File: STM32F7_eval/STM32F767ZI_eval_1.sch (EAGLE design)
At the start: 102 parts, among them CN1 STLINKV2_SWD_IF_, CN2 GROVE-4P-CONN-I2C-90D, CN3 GROVE-4P-CONN-I2C-90D, CN5 ARDUINO_COMPAT_IF, CN7 WFT0750CZ09-SMD_, CN9 UART_IF, Q1 PMF370XN_, SW1 SKRPACE010_, SW2 SKRPACE010_, U1 STM32F767ZI_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

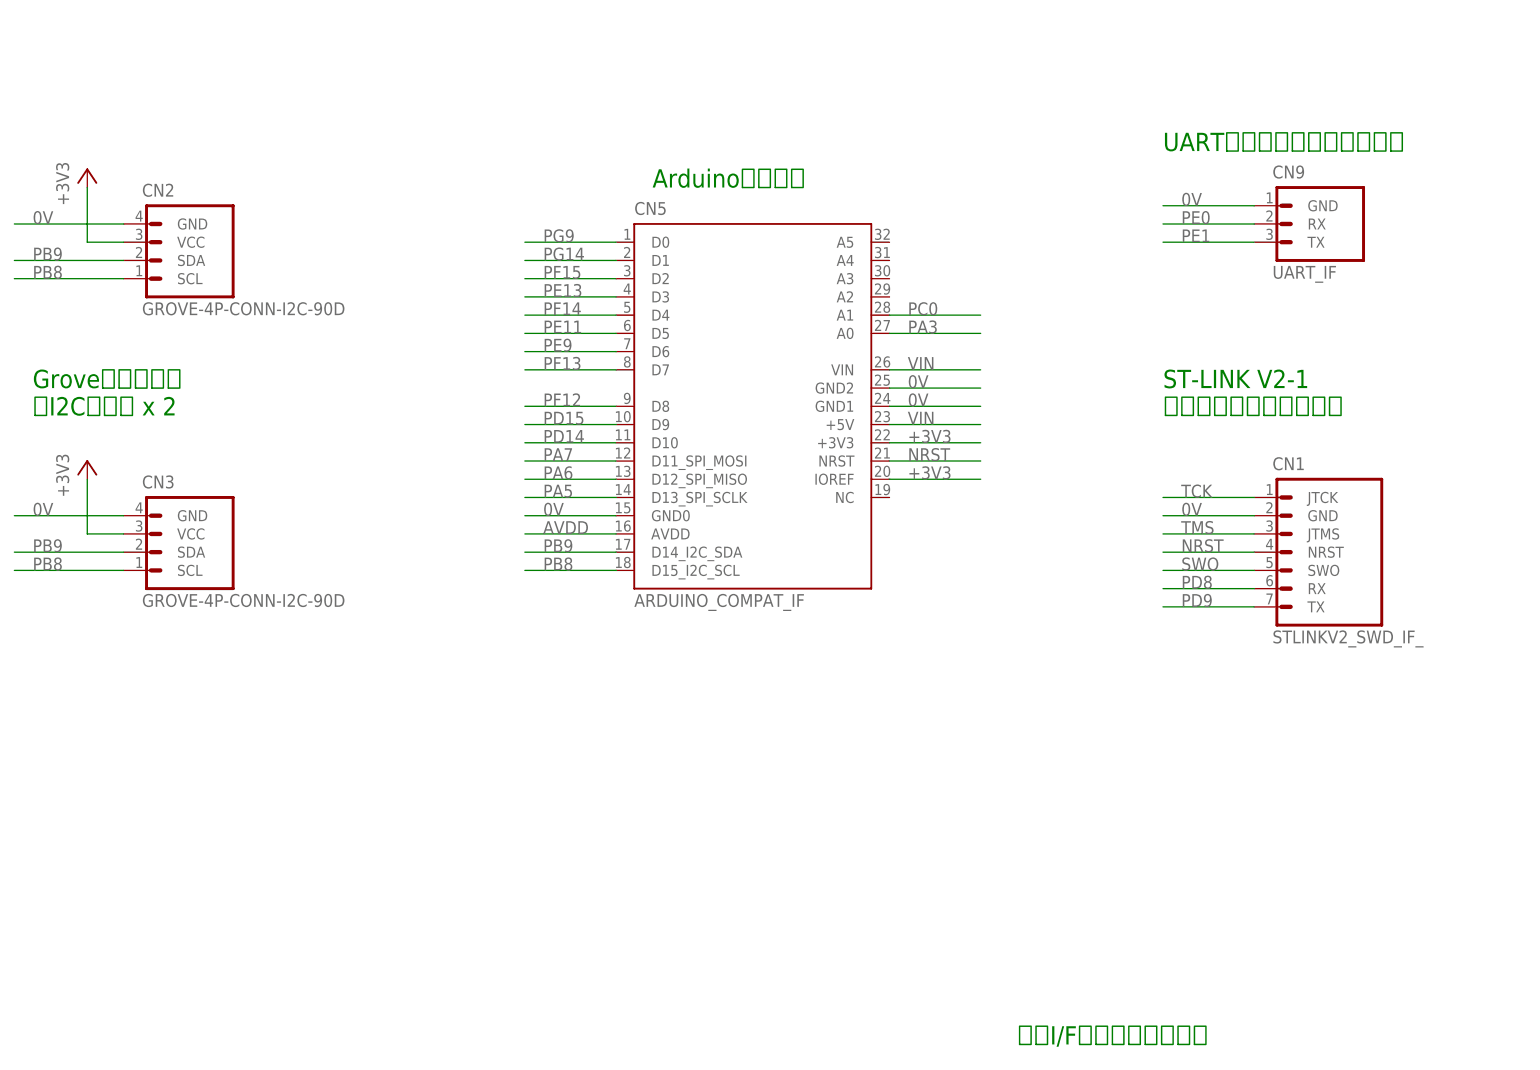
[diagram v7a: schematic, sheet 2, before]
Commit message: レイアウトを修正
・外部RX、TXはArduinoアナログピンを流用させるよう実装変更
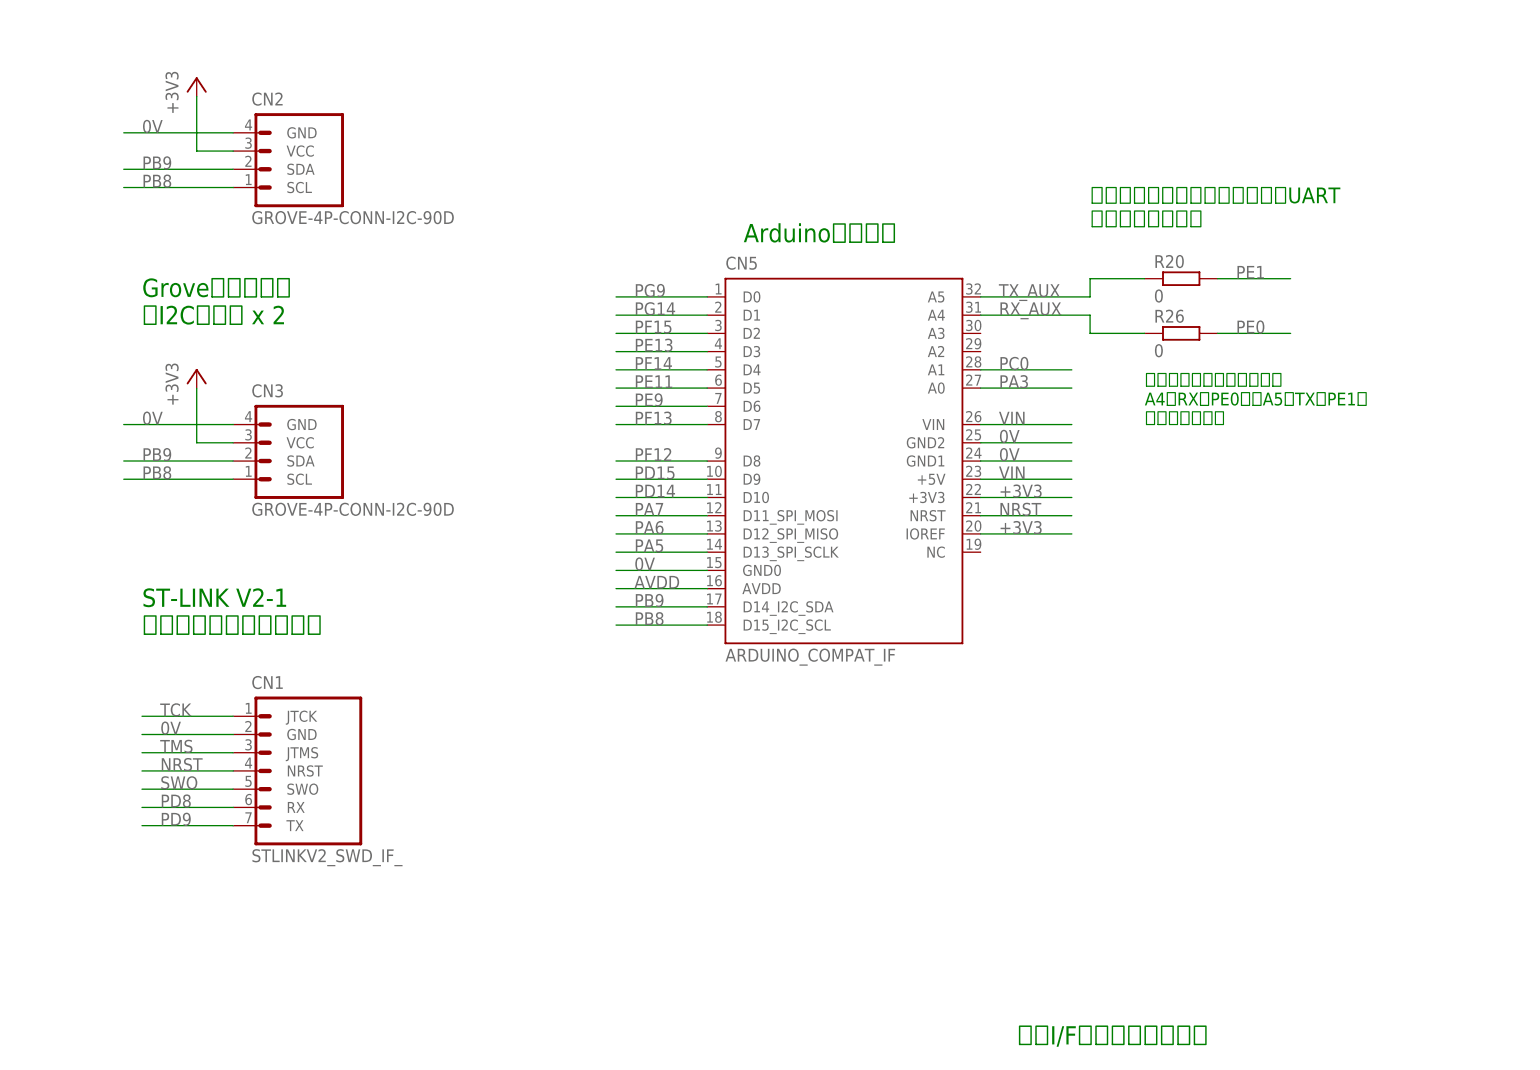
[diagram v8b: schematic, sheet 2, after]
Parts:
- removed CN9: UART_IF, PartsForProto:UART_IF
- added R20, R26: 0, Parts:RESISTOR_0603_DEV
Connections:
- new net RX_AUX: CN5.A4, R26.1
- new net TX_AUX: CN5.A5, R20.1
- net 0V: no longer CN9.GND
- net PE0: now also R26.2; no longer CN9.RX
- net PE1: now also R20.2; no longer CN9.TX
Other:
- note added: "ジャンパーを実装すると、 A4＝RX（PE0）、A5＝TX（PE1） に転化します。"
- note added: "通信モジュールメンテナンス用UART 接続用ジャンパー"
- note removed: "UARTインターフェース用ピン"
- moved on the sheet: CN1, CN2, CN3, CN5
